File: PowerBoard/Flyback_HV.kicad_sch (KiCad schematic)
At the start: 62 parts, among them J3 Molex Microfit 3.0, Q2 FDD86250-F085, Q3 FGH50T65SQD-F155, Q5 TN2130K1-G, Q6 STD11N60DM2, Q7 FGH50T65SQD-F155, T1 DA2034, U2 LT3750, U4 MCP14A0454-E/SN

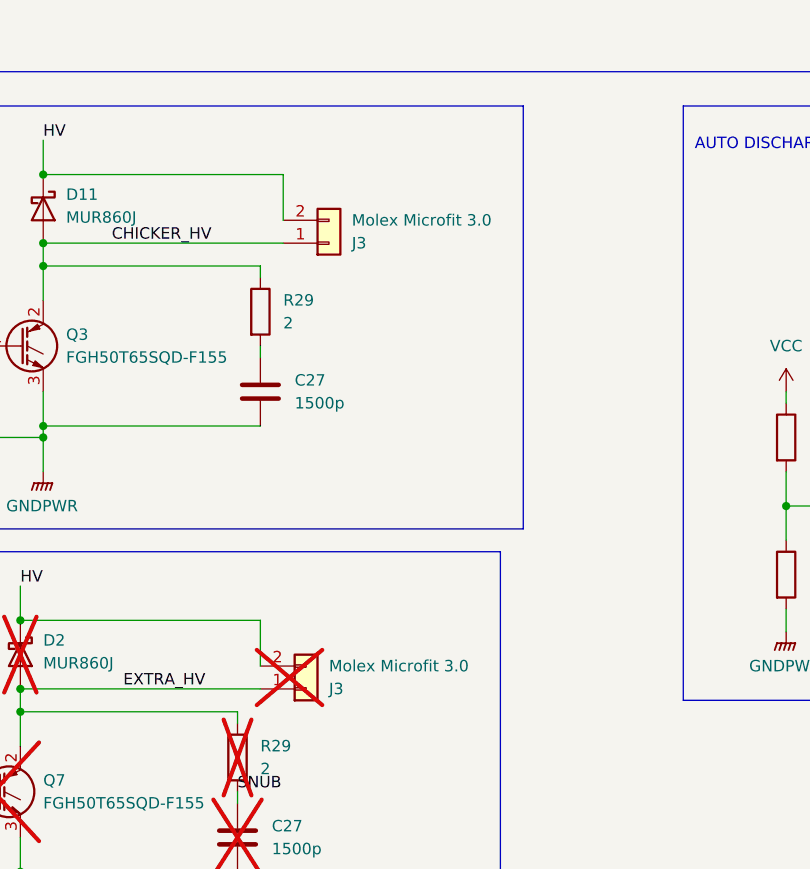
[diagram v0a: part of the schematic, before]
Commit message: powerboard HV powerpillars + midplate
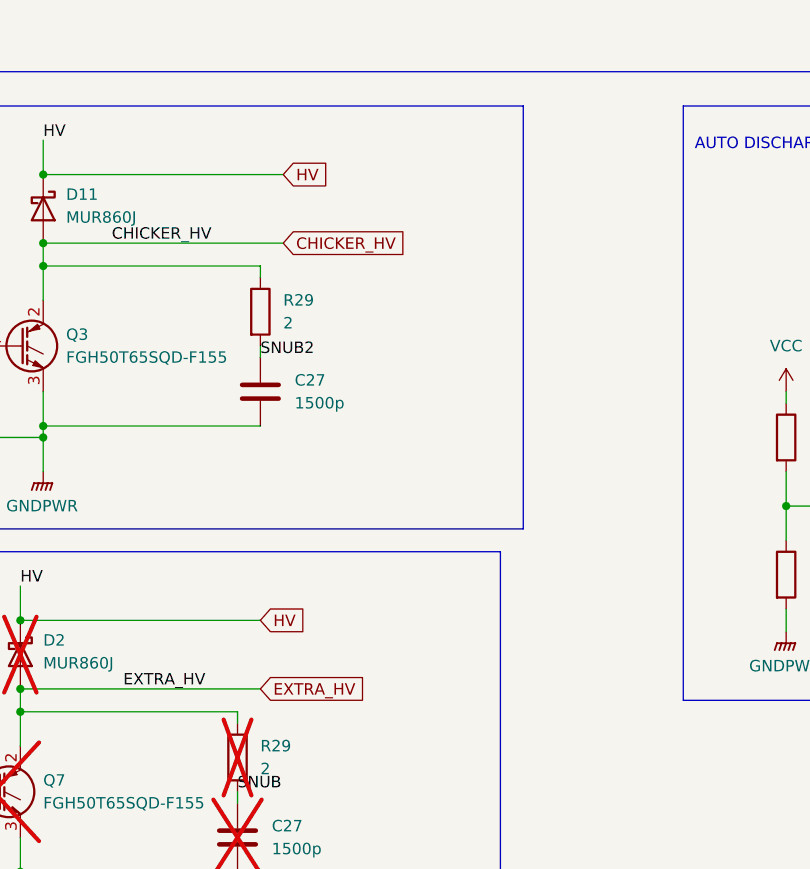
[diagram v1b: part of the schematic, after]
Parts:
- removed J3 (x2): Molex Microfit 3.0, bots:Molex_Micro-Fit_3.0_43650-0215_1x02_P3.00mm_Vertical, symbol bots:Molex_Microfit_3.0_1x2
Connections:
- net SNUB2: now reaches C27.1, R29.2
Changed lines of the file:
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@@
-    (stroke (width 0) (type default))
-  )
-  (wire (pts (xy 151.13 104.14) (xy 151.13 109.22))
     (stroke (width 0) (type default))
   )
@@
   )
   (wire (pts (xy 215.9 60.96) (xy 215.9 62.23))
-    (stroke (width 0) (type default))
-  )
-  (wire (pts (xy 148.59 153.67) (xy 148.59 158.75))
     (stroke (width 0) (type default))
   )
@@
     (effects (font (size 1.27 1.27)) (justify left bottom))
   )
+  (label "SNUB2" (at 148.59 124.46 0) (fields_autoplaced)
+    (effects (font (size 1.27 1.27)) (justify left bottom))
+  )
   (label "CHIP_EXTRA" (at 29.21 125.73 0) (fields_autoplaced)
     (effects (font (size 1.27 1.27)) (justify left bottom))
@@
   (label "VSOURCE" (at 104.14 67.31 0) (fields_autoplaced)
     (effects (font (size 1.27 1.27)) (justify left bottom))
+  )
+  (global_label "EXTRA_HV" (shape input) (at 148.59 161.29 0) (fields_autoplaced)
+    (effects (font (size 1.27 1.27)) (justify left))
+    (property "Intersheetrefs" "${INTERSHEET_REFS}" (at 160.6466 161.29 0)
+      (effects (font (size 1.27 1.27)) (justify left) hide)
+    )
   )
   (global_label "DONE" (shape input) (at 49.53 58.42 180) (fields_autoplaced)
@@
     )
   )
+  (global_label "CHICKER_HV" (shape input) (at 151.13 111.76 0) (fields_autoplaced)
+    (effects (font (size 1.27 1.27)) (justify left))
+    (property "Intersheetrefs" "${INTERSHEET_REFS}" (at 165.6662 111.76 0)
+      (effects (font (size 1.27 1.27)) (justify left) hide)
+    )
+  )
+  (global_label "HV" (shape input) (at 151.13 104.14 0) (fields_autoplaced)
+    (effects (font (size 1.27 1.27)) (justify left))
+    (property "Intersheetrefs" "${INTERSHEET_REFS}" (at 156.5343 104.14 0)
+      (effects (font (size 1.27 1.27)) (justify left) hide)
+    )
+  )
   (global_label "CHARGE" (shape input) (at 49.53 63.5 180) (fields_autoplaced)
     (effects (font (size 1.27 1.27)) (justify right))
     (property "Intersheetrefs" "${INTERSHEET_REFS}" (at 39.1667 63.5 0)
       (effects (font (size 1.27 1.27)) (justify right) hide)
+    )
+  )
+  (global_label "HV" (shape input) (at 148.59 153.67 0) (fields_autoplaced)
+    (effects (font (size 1.27 1.27)) (justify left))
+    (property "Intersheetrefs" "${INTERSHEET_REFS}" (at 153.9943 153.67 0)
+      (effects (font (size 1.27 1.27)) (justify left) hide)
     )
   )
@@
     )
   )
-  (symbol (lib_id "bots:Molex_Microfit_3.0_1x2") (at 153.67 161.29 0) (mirror x) (unit 1)
-    (in_bom yes) (on_board yes) (dnp yes)
-    (property "Reference" "J3" (at 156.21 161.29 0)
-      (effects (font (size 1.27 1.27)) (justify left))
-    )
-    (property "Value" "Molex Microfit 3.0" (at 156.21 158.75 0)
-      (effects (font (size 1.27 1.27)) (justify left))
-    )
-    (property "Footprint" "bots:Molex_Micro-Fit_3.0_43650-0215_1x02_P3.00mm_Vertical" (at 153.67 161.29 0)
-      (effects (font (size 1.27 1.27)) hide)
-    )
-    (property "Datasheet" "~" (at 153.67 161.29 0)
-      (effects (font (size 1.27 1.27)) hide)
-    )
-    (property "MPN" "0436500215" (at 153.67 161.29 0)
-      (effects (font (size 1.27 1.27)) hide)
-    )
-    (property "Manufacturer" "Molex" (at 153.67 161.29 0)
-      (effects (font (size 1.27 1.27)) hide)
-    )
-    (property "Price" "0.97" (at 153.67 161.29 0)
-      (effects (font (size 1.27 1.27)) hide)
-    )
-    (pin "1")
-    (pin "2")
-    (instances
-      (project "POWER_BOARD"
-        (path "/1a9ce3e8-a091-496c-9c5f-e7b2eb60e275"
-          (reference "J3") (unit 1)
-        )
-        (path "/1a9ce3e8-a091-496c-9c5f-e7b2eb60e275/aa68550e-c35d-4fef-b4e5-f1eb6225215f"
-          (reference "J3") (unit 1)
-        )
-      )
-    )
-  )
   (symbol (lib_id "power:GNDPWR") (at 248.92 142.24 0) (unit 1)
     (in_bom yes) (on_board yes) (dnp no) (fields_autoplaced)
@@
         )
       )
-    )
-  )
-  (symbol (lib_id "bots:Molex_Microfit_3.0_1x2") (at 156.21 111.76 0) (mirror x) (unit 1)
-    (in_bom yes) (on_board yes) (dnp no)
-    (property "Reference" "J3" (at 158.75 111.76 0)
-      (effects (font (size 1.27 1.27)) (justify left))
-    )
-    (property "Value" "Molex Microfit 3.0" (at 158.75 109.22 0)
-      (effects (font (size 1.27 1.27)) (justify left))
-    )
-    (property "Footprint" "bots:Molex_Micro-Fit_3.0_43650-0215_1x02_P3.00mm_Vertical" (at 156.21 111.76 0)
-      (effects (font (size 1.27 1.27)) hide)
-    )
-    (property "Datasheet" "~" (at 156.21 111.76 0)
-      (effects (font (size 1.27 1.27)) hide)
-    )
-    (property "MPN" "0436500215" (at 156.21 111.76 0)
-      (effects (font (size 1.27 1.27)) hide)
-    )
-    (property "Manufacturer" "Molex" (at 156.21 111.76 0)
-      (effects (font (size 1.27 1.27)) hide)
-    )
-    (property "Price" "0.97" (at 156.21 111.76 0)
-      (effects (font (size 1.27 1.27)) hide)
-    )
-    (pin "1")
-    (pin "2")
-    (instances
-      (project "POWER_BOARD"
-        (path "/1a9ce3e8-a091-496c-9c5f-e7b2eb60e275"
-          (reference "J3") (unit 1)
-        )
-        (path "/1a9ce3e8-a091-496c-9c5f-e7b2eb60e275/aa68550e-c35d-4fef-b4e5-f1eb6225215f"
-          (reference "J6") (unit 1)
-        )
-      )

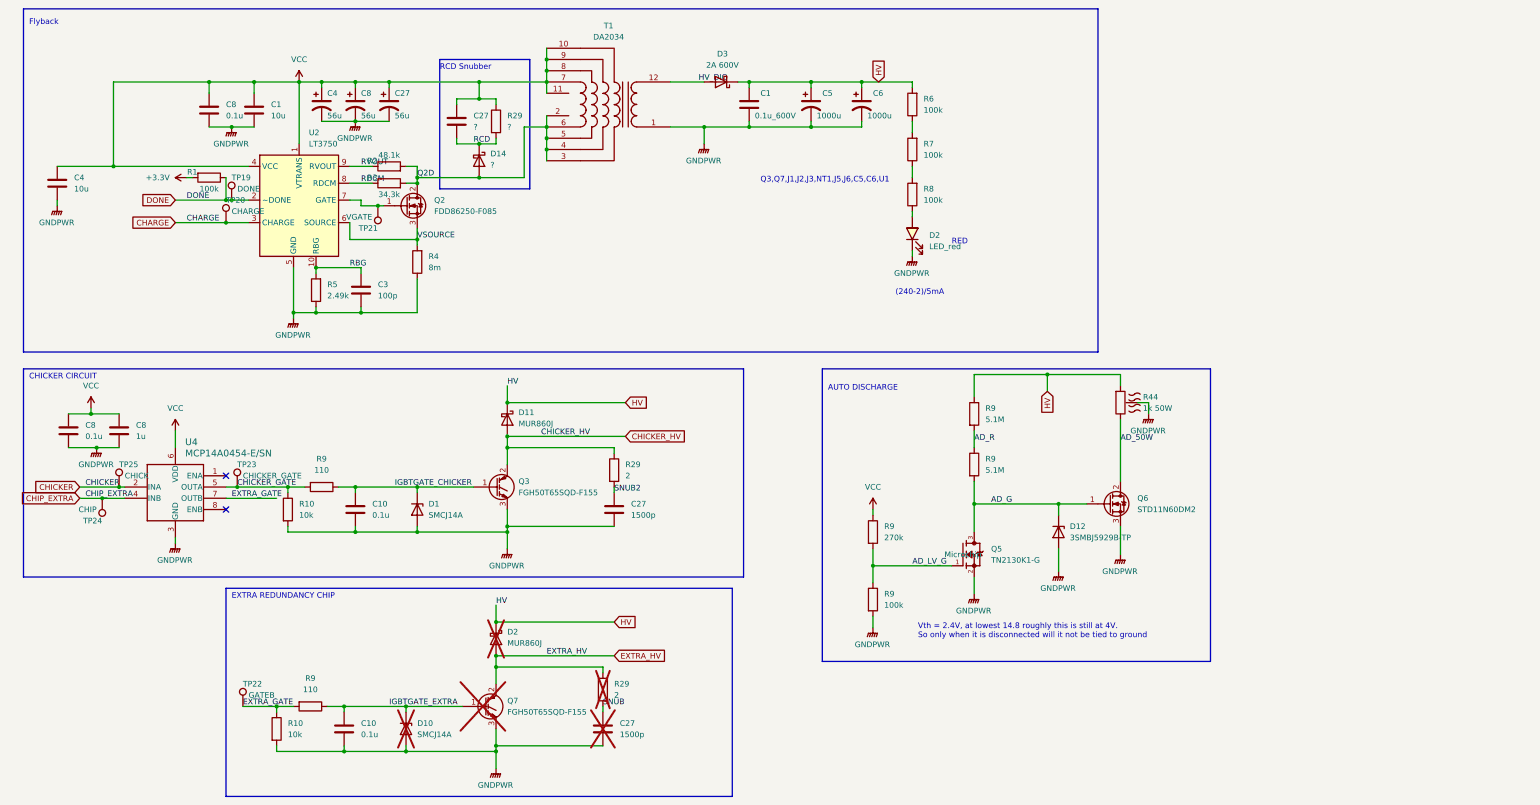
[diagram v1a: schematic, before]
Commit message: update to midplate and powerboard
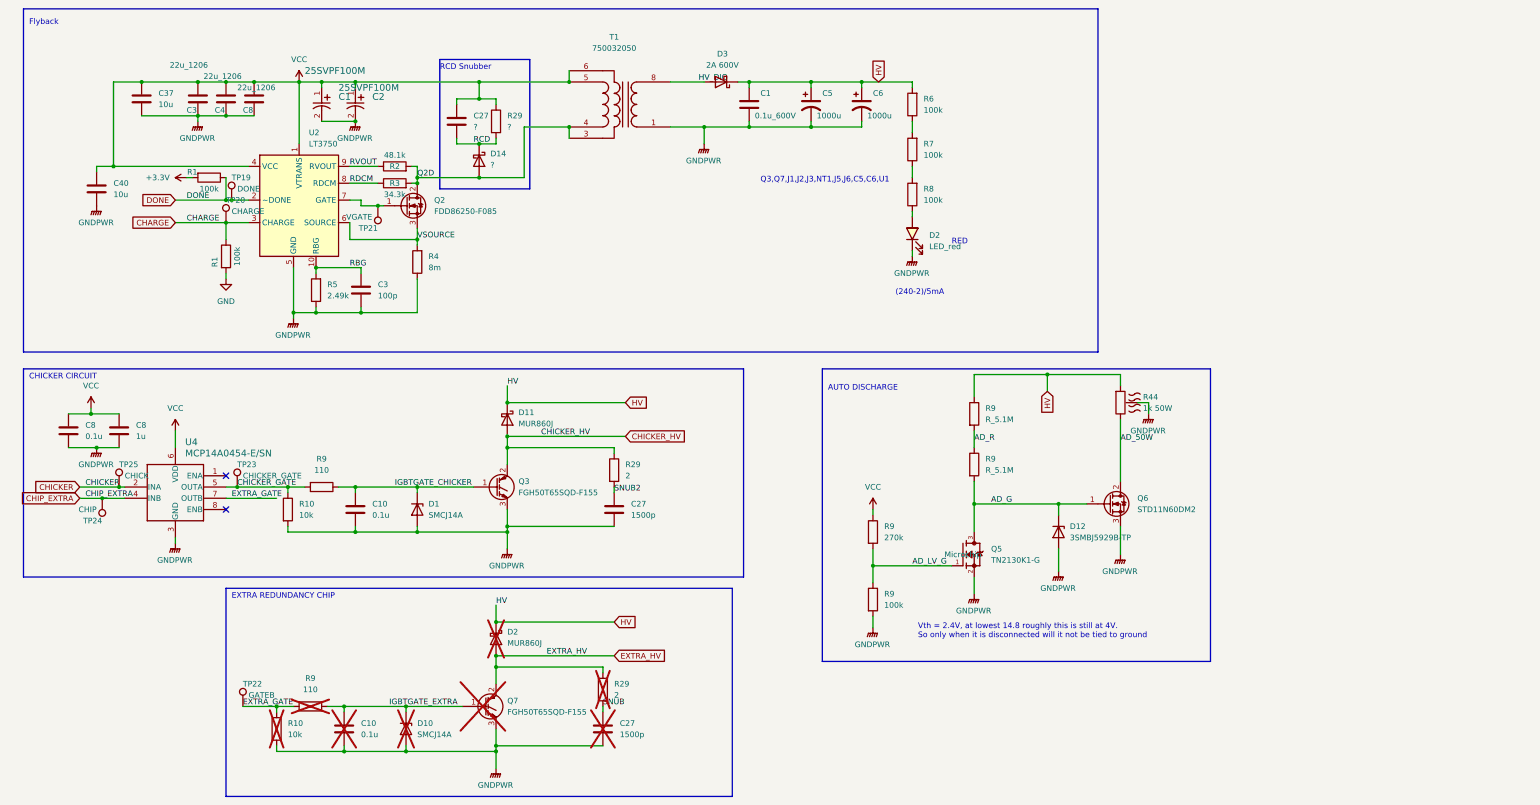
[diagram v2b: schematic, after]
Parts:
- removed C1, C4: 10u, bots:C_0805_2012Metric, symbol bots:C_10u
- removed C27, C4, C8: 56u, bots:CP_Elec_6.3x5.7, symbol bots:CAP_56uPOL
- removed C8: 0.1u, bots:C_0603_1608Metric, symbol bots:C_0.1u
- removed T1: DA2034, bots:DA2034-ALD_COC, symbol bots:DA2034
- added C1, C2: 25SVPF100M, bots:CAP_25SVPF100M, symbol bots:25SVPF100M
- added C3, C4, C8: 22u_1206, bots:C_1206_3216Metric, symbol bots:C_22u_1206
- added C37, C40: 10u, bots:C_0805_2012Metric, symbol bots:C_10u
- added R1: 100k, bots:R_0603_1608Metric, symbol bots:R_100k
- added T1: 750032050, bots:SMT_32050_WRE, symbol bots:Wurth_750032050
- C1: JLC Extended (none) -> yes; LCSC C342668 -> C2902776
- C10: JLC Extended (none) -> no; now not fitted; now left out of the parts list
- C10, C3, C8, R1, R6, R7, R8, R9: JLC Extended (none) -> no
- R10, R9: now not fitted; now left out of the parts list
- R9: value 5.1M -> R_5.1M; JLC Extended (none) -> yes
- R9: value 5.1M -> R_5.1M
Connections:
- net CHARGE: now also R1.1
- net GNDPWR: now also C1.2, C2.2, C3.2, C37.2, C4.2, C40.2, C8.2, T1.1 (VoutCOM)
- net HV_DIO: now also T1.8 (Vout)
- net Q2D: now also T1.3 (VinCOM2), T1.4 (VinCOM3)
- net VCC: now also C1.1, C2.1, C3.1, C37.1, C4.1, C40.1, C8.1, T1.5 (Vin1), T1.6 (Vin2)
- new net GND: R1.2
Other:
- moved on the sheet: R2, R3

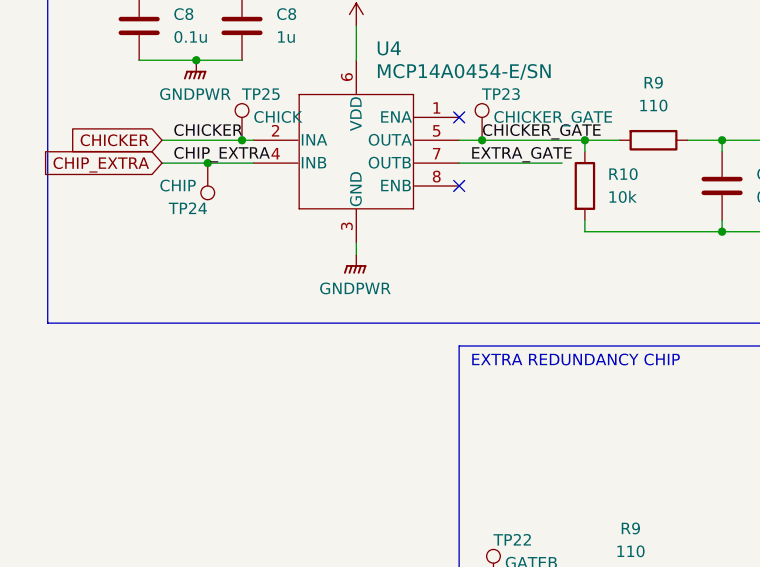
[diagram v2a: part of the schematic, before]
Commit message: update to midplate hole placements
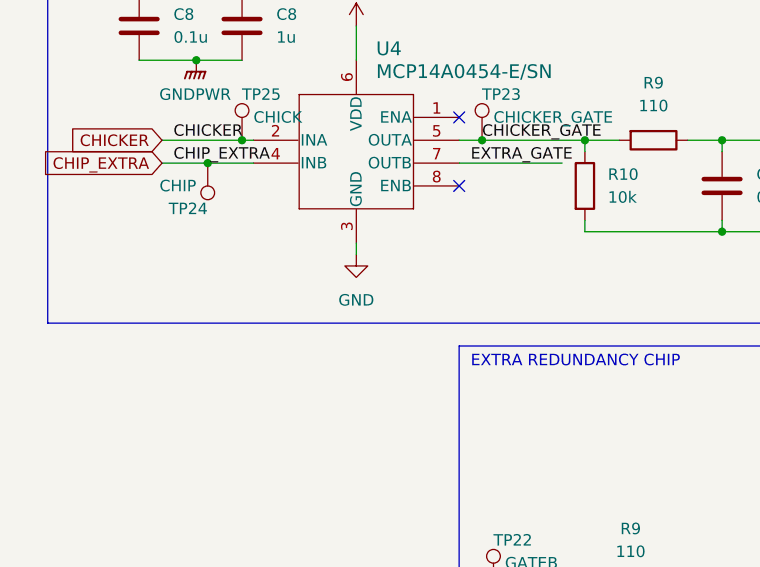
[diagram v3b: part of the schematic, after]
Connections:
- net GND: now also U4.3 (GND)
- net GNDPWR: no longer U4.3 (GND)
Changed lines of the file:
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@@
-    )
-  )
-  (symbol (lib_id "power:GNDPWR") (at 49.53 135.89 0) (unit 1)
-    (in_bom yes) (on_board yes) (dnp no) (fields_autoplaced)
-    (property "Reference" "#PWR04" (at 49.53 140.97 0)
-      (effects (font (size 1.27 1.27)) hide)
-    )
-    (property "Value" "GNDPWR" (at 49.403 139.7 0)
-      (effects (font (size 1.27 1.27)))
-    )
-    (property "Footprint" "" (at 49.53 137.16 0)
-      (effects (font (size 1.27 1.27)) hide)
-    )
-    (property "Datasheet" "" (at 49.53 137.16 0)
-      (effects (font (size 1.27 1.27)) hide)
-    )
-    (pin "1")
-    (instances
-      (project "POWER_BOARD"
-        (path "/1a9ce3e8-a091-496c-9c5f-e7b2eb60e275/aa68550e-c35d-4fef-b4e5-f1eb6225215f"
-          (reference "#PWR04") (unit 1)
-        )
-      )
     )
   )
@@
         )
       )
+    )
+  )
+  (symbol (lib_id "power:GND") (at 49.53 135.89 0) (unit 1)
+    (in_bom yes) (on_board yes) (dnp no) (fields_autoplaced)
+    (property "Reference" "#PWR?" (at 49.53 142.24 0)
+      (effects (font (size 1.27 1.27)) hide)
+    )
+    (property "Value" "GND" (at 49.53 140.97 0)
+      (effects (font (size 1.27 1.27)))
+    )
+    (property "Footprint" "" (at 49.53 135.89 0)
+      (effects (font (size 1.27 1.27)) hide)
+    )
+    (property "Datasheet" "" (at 49.53 135.89 0)
+      (effects (font (size 1.27 1.27)) hide)
+    )
+    (pin "1")
+    (instances
+      (project "POWER_BOARD"
+        (path "/1a9ce3e8-a091-496c-9c5f-e7b2eb60e275"
+          (reference "#PWR?") (unit 1)
+        )
+        (path "/1a9ce3e8-a091-496c-9c5f-e7b2eb60e275/13b16574-f046-4bb6-b573-f06681d59f31"
+          (reference "#PWR08") (unit 1)
+        )
+        (path "/1a9ce3e8-a091-496c-9c5f-e7b2eb60e275/44109b35-87db-4b37-b749-86ba1243ffef"
+          (reference "#PWR025") (unit 1)
+        )
+        (path "/1a9ce3e8-a091-496c-9c5f-e7b2eb60e275/aa68550e-c35d-4fef-b4e5-f1eb6225215f"
+          (reference "#PWR04") (unit 1)
+        )
+      )
